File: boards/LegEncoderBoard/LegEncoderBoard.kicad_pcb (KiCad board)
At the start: 2 copper layers, 34 x 42.5 mm, 5 parts, among them J1 S6B-PH-SM4-TB

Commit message: Pre-final leg encoder board
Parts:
- removed ENC1: AS5045-ASST, AS5045:SSOP16_AS5040-ASST_AMS
- added R1: 4.7K, Resistor4.7K:CR0603-FX-4701ELF, F.Cu at (141.8, 104.4)
- added R2: 4.7K, Resistor4.7K:CR0603-FX-4701ELF, F.Cu at (141.8, 103.0)
- added R3: 4.7K, Resistor4.7K:CR0603-FX-4701ELF, F.Cu at (141.8, 105.8)
- added U1: AS5047P-ATST, AS5047P-ASST:AS5047P-ASST, F.Cu at (147.0, 104.9)
- C1: value CC0805KKX5R7BB106 -> 100nF; footprint AS5045-3V3-REG-CAP:CAPC2012X70 -> Capacitor100nF:885342208002
- C2: value CC0805KRX7R7BB104 -> 10nF; footprint AS5045-DECOP-CAP:CC0805N_YAG -> Capacitor10nF:885012206089
- C3: value CC0402KRX7R7BB104 -> 1uF; footprint AS5045-PROG-CAP:YAG_CC0402_YAG -> Capacitor1uF:CC0603JRX7R7BB105
- J1: value S6B-PH-SM4-TB -> Conn_01x05; footprint JST-XH-6:CONN_S6B-XH-SM4-TB_JST -> Connector_JST:JST_XH_B5B-XH-A_1x05_P2.50mm_Vertical
- moved J1 33.5 mm to (142.2, 134.8)
- moved C3 30.4 mm to (153.2, 106.2), turned to 90 degrees
- moved C2 28.1 mm to (151.7, 106.2), turned to -90 degrees
- moved C1 24.0 mm to (153.2, 103.5)
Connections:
- C1 pad 1: GND -> VIN
- C1 pad 2: Net-(ENC1-VDD3V3) -> GND
- C2 pad 1: +5V -> VIN
- C3 pad 1: Net-(ENC1-PROG) -> GND
- C3 pad 2: GND -> VIN
- J1 pad 1: +5V -> VIN
- J1 pad 2: Net-(ENC1-CSN) -> A
- J1 pad 3: Net-(ENC1-CLK) -> B
- J1 pad 4: Net-(ENC1-DO) -> I
- J1 pad 5: Net-(ENC1-PROG) -> GND
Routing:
- net VIN: track 0.00 -> 50.6 mm
- net I: track 0.00 -> 38.2 mm
- net A: track 0.00 -> 36.2 mm
- net Net-(ENC1-PROG): track 33.5 -> 0.00 mm
- net B: track 0.00 -> 31.4 mm
- net +5V: track 28.0 -> 0.00 mm
- net Net-(ENC1-CSN): track 18.7 -> 0.00 mm
- net Net-(ENC1-CLK): track 17.0 -> 0.00 mm
- net Net-(ENC1-DO): track 15.3 -> 0.00 mm
- net Net-(ENC1-VDD3V3): track 10.7 -> 0.00 mm, vias 2 -> 0
- net GND: track 10.1 -> 0.00 mm, vias 3 -> 0
- net MOSI: track 0.00 -> 2.01 mm
- net SCK: track 0.00 -> 1.99 mm
- net CS: track 0.00 -> 1.70 mm
- added copper zone on F.Cu, net GND
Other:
- board size 34 x 42.5 mm -> 76.2 x 76.2 mm
- board text removed: "5V"
- board text removed: "CK"
- board text removed: "CS"
- board text removed: "DI"
- board text removed: "DO"
- board text removed: "GND"

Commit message: Leg encoder board pre-final
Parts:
- added C4: 0.1uF, Capacitor0.1uF:GRM188R71H104KA93J, F.Cu at (137.7, 106.2)
- added C5: 1uF, Capacitor1uF:CC0603JRX7R7BB105, F.Cu at (129.1, 111.1)
- added C6: 1uF, Capacitor1uF:CC0603JRX7R7BB105, F.Cu at (155.8, 111.1)
- added C7: 1uF, Capacitor1uF:CC0603JRX7R7BB105, F.Cu at (142.4, 111.1)
- added CR1: BAT54, EnvelopeDiode:BAT54WS-7-F, F.Cu at (129.4, 114.2)
- added CR2: BAT54, EnvelopeDiode:BAT54WS-7-F, F.Cu at (156.1, 114.3)
- added CR3: BAT54, EnvelopeDiode:BAT54WS-7-F, F.Cu at (142.7, 114.2)
- added D1: REDLED, RedLED:RC0603FR-07150RL, F.Cu at (147.1, 89.5)
- added D2: BLUELED, BlueLED:150080BS75000_Modified, F.Cu at (137.9, 89.5)
- added D3: BLUELED, BlueLED:150080BS75000_Modified, F.Cu at (156.2, 89.5)
- added H1: MountingHole, MountingHole:MountingHole_2.5mm_Pad, F.Cu at (126.1, 83.9)
- added H2: MountingHole, MountingHole:MountingHole_2.5mm_Pad, F.Cu at (168.1, 83.9)
- added H3: MountingHole, MountingHole:MountingHole_2.5mm_Pad, F.Cu at (126.1, 125.9)
- added H4: MountingHole, MountingHole:MountingHole_2.5mm_Pad, F.Cu at (168.1, 125.9)
- added Q1: MMBT3904, Transistor:MMBT3904LT1G, F.Cu at (137.6, 111.1)
- added Q2: MMBT3904, Transistor:MMBT3904LT1G, F.Cu at (164.3, 111.1)
- added Q3: MMBT3904, Transistor:MMBT3904LT1G, F.Cu at (151.0, 111.1)
- added R10: 100K, Resistor100K:CRCW0603100KFKEA, F.Cu at (144.4, 111.1)
- added R11: 47K, Resistor47K:RC0603FR-0747KL, F.Cu at (146.2, 111.1)
- added R12: 470K, Resistor470K:RC0603FR-07470KL, F.Cu at (147.8, 111.1)
- added R13: 22R, Resistor22:RC0603FR-0722RL, F.Cu at (133.9, 106.3)
- added R14: 22R, Resistor22:RC0603FR-0722RL, F.Cu at (133.9, 103.1)
- added R15: 22R, Resistor22:RC0603FR-0722RL, F.Cu at (133.9, 104.7)
- added R4: 1K, Resistor1K:RCG06031K00FKEA, F.Cu at (146.8, 114.2)
- added R5: 100K, Resistor100K:CRCW0603100KFKEA, F.Cu at (157.8, 111.1)
- added R6: 150R, Resistor150:RESC1607X60N, F.Cu at (133.6, 114.2)
- added R7: 47K, Resistor47K:RC0603FR-0747KL, F.Cu at (159.5, 111.1)
- added R8: 470K, Resistor470K:RC0603FR-07470KL, F.Cu at (161.1, 111.1)
- added R9: 150R, Resistor150:RESC1607X60N, F.Cu at (160.2, 114.3)
- added U2: SN74LVC3G17DCUR, SchmittBuffer:SN74LVC3G17DCUR, F.Cu at (137.7, 103.8)
- J1: footprint Connector_JST:JST_XH_B5B-XH-A_1x05_P2.50mm_Vertical -> Connector_IDC:IDC-Header_2x04_P2.54mm_Vertical
- R1: value 4.7K -> 100K; footprint Resistor4.7K:CR0603-FX-4701ELF -> Resistor100K:CRCW0603100KFKEA
- R2: value 4.7K -> 47K; footprint Resistor4.7K:CR0603-FX-4701ELF -> Resistor47K:RC0603FR-0747KL
- R3: value 4.7K -> 470K; footprint Resistor4.7K:CR0603-FX-4701ELF -> Resistor470K:RC0603FR-07470KL
- moved J1 13.2 mm to (151.1, 125.1), turned to -90 degrees
- moved R1 12.6 mm to (131.0, 111.1), turned to -90 degrees
- moved R2 12.0 mm to (132.8, 111.1), turned to -90 degrees
- moved R3 9.13 mm to (134.4, 111.1), turned to -90 degrees
- moved C3 1.01 mm to (154.2, 106.3)
- moved C2 0.81 mm to (152.4, 106.4)
- moved C1 0.80 mm to (154.0, 103.5)
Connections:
- J1 pad 2: A -> GND
- J1 pad 3: B -> /A_OUT
- J1 pad 4: I -> GND
- J1 pad 5: GND -> /B_OUT
- R1 pad 1: SCK -> /A_ENV
- R2 pad 1: VIN -> /A_ENV
- R2 pad 2: CS -> /A_BASE
- R3 pad 1: MOSI -> /A_BASE
- U1 pad 1: CS -> VIN
- U1 pad 2: SCK -> GND
- U1 pad 3: MISO -> unconnected-(U1-MISO-Pad3)
- U1 pad 4: MOSI -> GND
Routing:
- net VIN: track 50.6 -> 95.2 mm, vias 0 -> 1
- net /A_OUT: track 0.00 -> 37.2 mm
- net /B_OUT: track 0.00 -> 37.0 mm, vias 0 -> 1
- net A_BUF: track 0.00 -> 33.9 mm, vias 0 -> 2
- net B_BUF: track 0.00 -> 31.0 mm, vias 0 -> 2
- net /A_LED_ANODE: track 0.00 -> 29.0 mm, vias 0 -> 2
- net /I_OUT: track 0.00 -> 28.8 mm, vias 0 -> 1
- net A: track 36.2 -> 9.26 mm
- net /B_LED_ANODE: track 0.00 -> 26.7 mm, vias 0 -> 2
- net /B_LED_CATHODE: track 0.00 -> 25.8 mm
- net /A_LED_CATHODE: track 0.00 -> 25.5 mm, vias 0 -> 2
- net /I_LED_ANODE: track 0.00 -> 25.2 mm, vias 0 -> 2
- net GND: track 0.00 -> 25.2 mm, vias 0 -> 13
- net B: track 31.4 -> 6.73 mm
- net /I_LED_CATHODE: track 0.00 -> 23.9 mm
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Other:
- board size 76.2 x 76.2 mm -> 66 x 66 mm
- board text added: "3V3"
- board text added: "A"
- board text added: "B"
- board text added: "GND"
- board text added: "I"

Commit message: Prepare encoder boards for manufacturing
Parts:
- C1: footprint Capacitor100nF:885342208002 -> Capacitor100nF:CC0603KRX7R9BB104
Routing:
- net VIN: track 95.2 -> 96.2 mm
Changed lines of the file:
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@@
 			)
 		)
-		(property "LCSC" "C2169542"
+		(property "LCSC" "C85973"
 			(at 0 0 0)
 			(layer "F.SilkS")
@@
 		(embedded_fonts no)
 	)
-	(footprint "Capacitor100nF:885342208002"
+	(footprint "Capacitor100nF:CC0603KRX7R9BB104"
 		(layer "F.Cu")
 		(at 154 103.55)
+		(tags "CC0603KRX7R9BB104 ")
 		(property "Reference" "C1"
-			(at 0 -1.6032 0)
+			(at 0 0 0)
+			(unlocked yes)
 			(layer "F.SilkS")
 			(hide yes)
 			(effects
 				(font
-					(size 0.32 0.32)
-					(thickness 0.08)
+					(size 1 1)
+					(thickness 0.15)
 				)
 			)
 		)
 		(property "Value" "100nF"
-			(at -0.1 1.3968 0)
+			(at 0 0 0)
+			(unlocked yes)
 			(layer "F.Fab")
 			(hide yes)
 			(effects
 				(font
-					(size 0.32 0.32)
-					(thickness 0.08)
+					(size 1 1)
+					(thickness 0.15)
 				)
 			)
@@
 		(property "LCSC" "C2176910"
 			(at 0 0 0)
-			(layer "F.SilkS")
+			(unlocked yes)
+			(layer "F.Fab")
 			(hide yes)
 			(effects
 				(font
-					(size 1.27 1.27)
+					(size 1 1)
 					(thickness 0.15)
 				)
@@
 		(attr smd)
 		(fp_line
-			(start -0.8 -0.9)
-			(end 0.8 -0.9)
+			(start -1.1049 -0.5334)
+			(end 1.1049 -0.5334)
 			(stroke
-				(width 0.2)
+				(width 0.1524)
 				(type solid)
 			)
-			(layer "F.SilkS")
+			(layer "F.CrtYd")
 		)
 		(fp_line
-			(start 0.8 0.9)
-			(end -0.8 0.9)
+			(start -1.1049 0.5334)
+			(end -1.1049 -0.5334)
 			(stroke
-				(width 0.2)
+				(width 0.1524)
 				(type solid)
 			)
-			(layer "F.SilkS")
+			(layer "F.CrtYd")
 		)
-		(fp_poly
-			(pts
-				(xy -2.2 -1.1) (xy 2.2 -1.1) (xy 2.2 1.1) (xy -2.2 1.1)
+		(fp_line
+			(start 1.1049 -0.5334)
+			(end 1.1049 0.5334)
+			(stroke
+				(width 0.1524)
+				(type solid)
 			)
+			(layer "F.CrtYd")
+		)
+		(fp_line
+			(start 1.1049 0.5334)
+			(end -1.1049 0.5334)
 			(stroke
-				(width 0.1)
+				(width 0.1524)
 				(type solid)
 			)
-			(fill yes)
 			(layer "F.CrtYd")
 		)
 		(fp_line
-			(start -1.6 -0.8)
-			(end -1.6 0.8)
+			(start -0.8509 -0.4572)
+			(end -0.8509 0.4572)
 			(stroke
-				(width 0.1)
+				(width 0.0254)
 				(type solid)
 			)
@@
 		)
 		(fp_line
-			(start -1.6 -0.8)
-			(end 1.6 -0.8)
+			(start -0.8509 -0.4572)
+			(end -0.8509 0.4572)
 			(stroke
-				(width 0.1)
+				(width 0.0254)
 				(type solid)
 			)
@@
 		)
 		(fp_line
-			(start -1.6 0.8)
-			(end 1.6 0.8)
+			(start -0.8509 0.4572)
+			(end -0.2413 0.4572)
 			(stroke
-				(width 0.1)
+				(width 0.0254)
 				(type solid)
 			)
@@
 		)
 		(fp_line
-			(start 1.6 0.8)
-			(end 1.6 -0.8)
+			(start -0.8509 0.4572)
+			(end 0.8509 0.4572)
 			(stroke
-				(width 0.1)
+				(width 0.0254)
+				(type solid)
+			)
+			(layer "F.Fab")
+		)
+		(fp_line
+			(start -0.2413 -0.4572)
+			(end -0.8509 -0.4572)
+			(stroke
+				(width 0.0254)
+				(type solid)
+			)
+			(layer "F.Fab")
+		)
+		(fp_line
+			(start -0.2413 0.4572)
+			(end -0.2413 -0.4572)
+			(stroke
+				(width 0.0254)
+				(type solid)
+			)
+			(layer "F.Fab")
+		)
+		(fp_line
+			(start 0.2413 -0.4572)
+			(end 0.2413 0.4572)
+			(stroke
+				(width 0.0254)
+				(type solid)
+			)
+			(layer "F.Fab")
+		)
+		(fp_line
+			(start 0.2413 0.4572)
+			(end 0.8509 0.4572)
+			(stroke
+				(width 0.0254)
 				(type solid)
 			)
 			(layer "F.Fab")
 		)
+		(fp_line
+			(start 0.8509 -0.4572)
+			(end -0.8509 -0.4572)
+			(stroke
+				(width 0.0254)
+				(type solid)
+			)
+			(layer "F.Fab")
+		)
+		(fp_line
+			(start 0.8509 -0.4572)
+			(end 0.2413 -0.4572)
+			(stroke
+				(width 0.0254)
+				(type solid)
+			)
+			(layer "F.Fab")
+		)
+		(fp_line
+			(start 0.8509 0.4572)
+			(end 0.8509 -0.4572)
+			(stroke
+				(width 0.0254)
+				(type solid)
+			)
+			(layer "F.Fab")
+		)
+		(fp_line
+			(start 0.8509 0.4572)
+			(end 0.8509 -0.4572)
+			(stroke
+				(width 0.0254)
+				(type solid)
+			)
+			(layer "F.Fab")
+		)
+		(fp_text user "${REFERENCE}"
+			(at 0 0 0)
+			(unlocked yes)
+			(layer "F.Fab")
+			(effects
+				(font
+					(size 1 1)
+					(thickness 0.15)
+				)
+			)
+		)
 		(pad "1" smd rect
-			(at -1.55 0)
-			(size 0.9 1.6)
+			(at -0.6223 0)
+			(size 0.762 0.8636)
 			(layers "F.Cu" "F.Mask" "F.Paste")
 			(net 2 "VIN")
 			(pintype "passive")
-			(solder_mask_margin 0.102)
 		)
 		(pad "2" smd rect
-			(at 1.55 0)
-			(size 0.9 1.6)
+			(at 0.6223 0)
+			(size 0.762 0.8636)
 			(layers "F.Cu" "F.Mask" "F.Paste")
 			(net 7 "GND")
 			(pintype "passive")
-			(solder_mask_margin 0.102)
+		)
+		(zone
+			(net 0)
+			(net_name "")
+			(layer "F.Cu")
+			(hatch full 0.508)
+			(connect_pads
+				(clearance 0)
+			)
+			(min_thickness 0.254)
+			(filled_areas_thickness no)
+			(keepout
+				(tracks not_allowed)
+				(vias not_allowed)
+				(pads allowed)
+				(copperpour not_allowed)
+				(footprints allowed)
+			)
+			(placement
+				(enabled no)
+				(sheetname "")
+			)
+			(fill
+				(thermal_gap 0.508)
+				(thermal_bridge_width 0.508)
+			)
+			(polygon
+				(pts
+					(xy 153.8095 103.1436) (xy 154.1905 103.1436) (xy 154.1905 103.9564) (xy 153.8095 103.9564)
+				)
+			)
 		)
 		(embedded_fonts no)
-		(model "${KIPRJMOD}/dependencies/Capacitor100nF/885342208002.step"
+		(model "${KIPRJMOD}/dependencies/Capacitor100nF/CC0603KRX7R9BB104.step"
 			(offset
 				(xyz 0 0 0)
@@
 		(sheetname "/")
 		(sheetfile "LegEncoderBoard.kicad_sch")
-		(attr through_hole)
+		(attr through_hole exclude_from_pos_files exclude_from_bom)
 		(fp_line
 			(start -3.29 12.83)
@@
 		(width 0.25)
 		(layer "F.Cu")
+		(net 2)
+	)
+	(segment
+		(start 152.45 103.55)
+		(end 153.3777 103.55)
+		(width 0.25)
+		(layer "F.Cu")

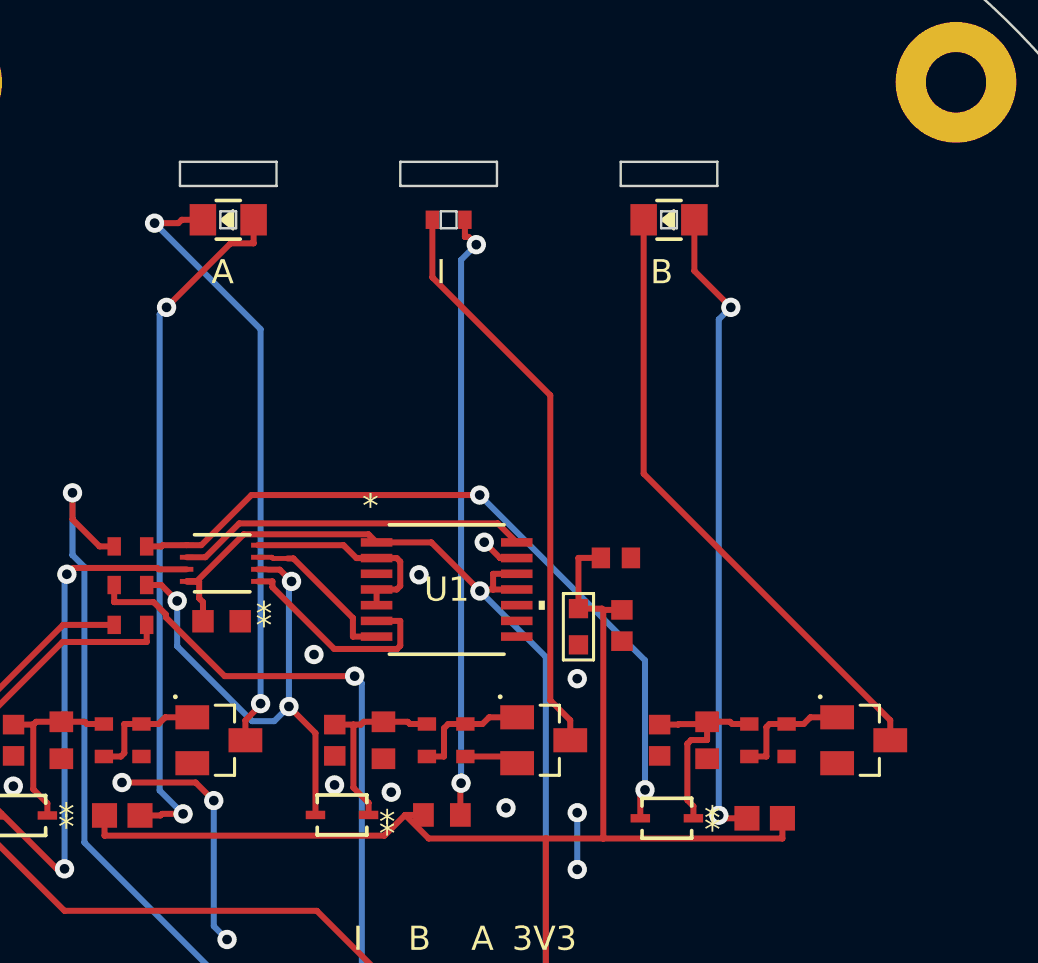
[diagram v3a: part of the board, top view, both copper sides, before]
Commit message: Pre-flight on two encoder boards
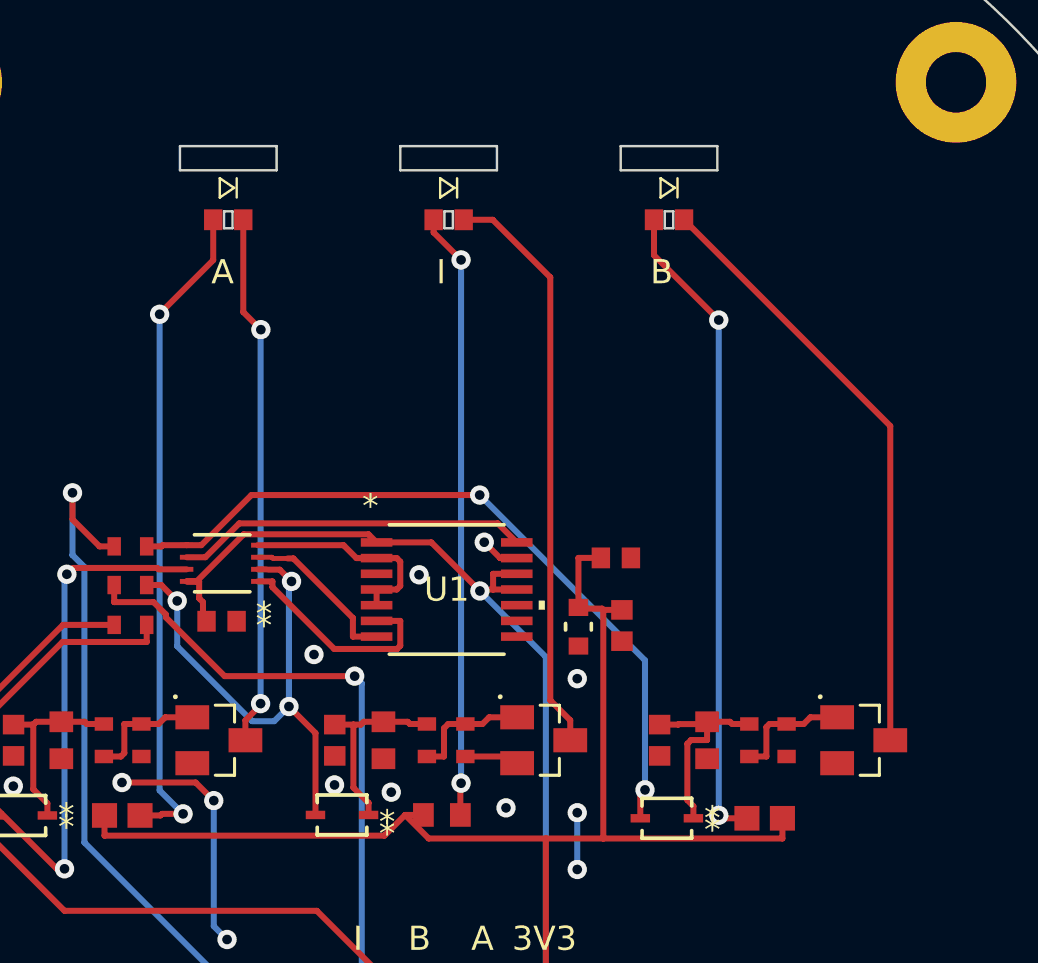
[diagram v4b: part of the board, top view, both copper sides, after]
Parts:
- C2: footprint Capacitor10nF:885012206089 -> Capacitor10nF:GRM1885C1H103JA01D
- C4: value 0.1uF -> 100nF; footprint Capacitor0.1uF:GRM188R71H104KA93J -> Capacitor100nF:CC0603KRX7R9BB104
- D1: footprint RedLED:RC0603FR-07150RL -> LedRed:YLED0603R
- D2, D3: footprint BlueLED:150080BS75000_Modified -> LedBlue:YLED0603B
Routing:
- net /A_LED_CATHODE: track 25.5 -> 22.1 mm
- net /A_LED_ANODE: track 29.0 -> 27.9 mm
- net /B_LED_CATHODE: track 25.8 -> 25.1 mm
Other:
- outline, holes or cut-outs redrawn

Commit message: Ordered leg encoder board
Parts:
- D1: footprint LedRed:YLED0603R -> LedRed:NCD0603R1
- D2, D3: footprint LedBlue:YLED0603B -> LedBlue:150080BS75000_Modified
- U2: value SN74LVC3G17DCUR -> SN74LVC3G17DCTR; footprint SchmittBuffer:SN74LVC3G17DCUR -> SchmittBuffer:SN74LVC3G17DCTR
- moved R15 6.49 mm to (140.1, 106.8)
- moved C4 3.85 mm to (133.8, 105.7), turned to 0 degrees
- moved R13 2.20 mm to (133.8, 104.1)
- moved U2 0.75 mm to (138.4, 103.8)
- moved R14 0.50 mm to (133.8, 102.6)
- turned D1 to 180 degrees
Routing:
- net GND: track 25.2 -> 46.3 mm, vias 13 -> 14
- net A_BUF: track 33.9 -> 17.4 mm, vias 2 -> 0
- net VIN: track 96.2 -> 83.2 mm, vias 1 -> 0
- net I_BUF: track 21.3 -> 12.3 mm, vias 3 -> 0
- net /I_OUT: track 28.8 -> 20.1 mm
- net /A_LED_CATHODE: track 22.1 -> 28.5 mm
- net /A_OUT: track 37.2 -> 32.8 mm, vias 0 -> 1
- net /A_LED_ANODE: track 27.9 -> 31.8 mm
- net B_BUF: track 31.0 -> 33.8 mm, vias 2 -> 0
- net /I_BASE: track 5.09 -> 7.03 mm
- net /B_LED_ANODE: track 27.0 -> 28.7 mm
- net /I_ENV: track 7.90 -> 9.27 mm
- net A: track 9.26 -> 7.99 mm
- net /I_LED_ANODE: track 25.1 -> 26.1 mm
- net B: track 6.73 -> 6.00 mm
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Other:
- outline, holes or cut-outs redrawn

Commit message: Finalize leg encoder board iteration
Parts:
- added C10: 10nF, Capacitor10nF:GRM1885C1H103JA01D, F.Cu at (140.7, 117.5)
- added C8: 10nF, Capacitor10nF:GRM1885C1H103JA01D, F.Cu at (132.9, 117.5)
- added C9: 10nF, Capacitor10nF:GRM1885C1H103JA01D, F.Cu at (165.4, 117.5)
- added CR4: BAT54, EnvelopeDiode:BAT54WS-7-F, F.Cu at (129.2, 117.5)
- added CR5: BAT54, EnvelopeDiode:BAT54WS-7-F, F.Cu at (161.6, 117.5)
- added CR6: BAT54, EnvelopeDiode:BAT54WS-7-F, F.Cu at (136.9, 117.5)
- added J2: Conn_01x04, Connector_JST:JST_XH_B4B-XH-A_1x04_P2.50mm_Vertical, F.Cu at (143.3, 81.6)
- added R16: 100K, Resistor100K:CRCW0603100KFKEA, F.Cu at (131.1, 117.5)
- added R17: 100K, Resistor100K:CRCW0603100KFKEA, F.Cu at (163.6, 117.5)
- added R18: 100K, Resistor100K:CRCW0603100KFKEA, F.Cu at (138.9, 117.5)
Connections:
- CR1 pad 2: A_BUF -> /A_PULSE
- CR2 pad 2: B_BUF -> /B_PULSE
- CR3 pad 2: I_BUF -> /I_PULSE
- U1 pad 1: VIN -> CS
- U1 pad 2: GND -> CLK
- U1 pad 3: unconnected-(U1-MISO-Pad3) -> MISO
- U1 pad 4: GND -> MOSI
- U1 pad 6: A -> B
- U1 pad 7: B -> A
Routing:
- net CLK: track 0.00 -> 56.8 mm, vias 0 -> 1
- net MOSI: track 0.00 -> 31.5 mm, vias 0 -> 1
- net MISO: track 0.00 -> 30.3 mm, vias 0 -> 1
- net CS: track 0.00 -> 25.1 mm, vias 0 -> 2
- net B_BUF: track 33.8 -> 54.2 mm, vias 0 -> 2
- net /B_PULSE: track 0.00 -> 14.0 mm, vias 0 -> 2
- net GND: track 46.3 -> 58.5 mm, vias 14 -> 19
- net /I_PULSE: track 0.00 -> 10.5 mm
- net I_BUF: track 12.3 -> 21.3 mm, vias 0 -> 2
- net /A_PULSE: track 0.00 -> 8.66 mm, vias 0 -> 2
- net A_BUF: track 17.4 -> 25.6 mm
- net A: track 7.99 -> 4.73 mm
- net /A_OUT: track 32.8 -> 34.9 mm
- net VIN: track 83.2 -> 84.5 mm
- net /A_LED_ANODE: track 31.8 -> 33.0 mm
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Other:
- board text added: "CLK"
- board text added: "CS"
- board text added: "MISO"
- board text added: "MOSI"

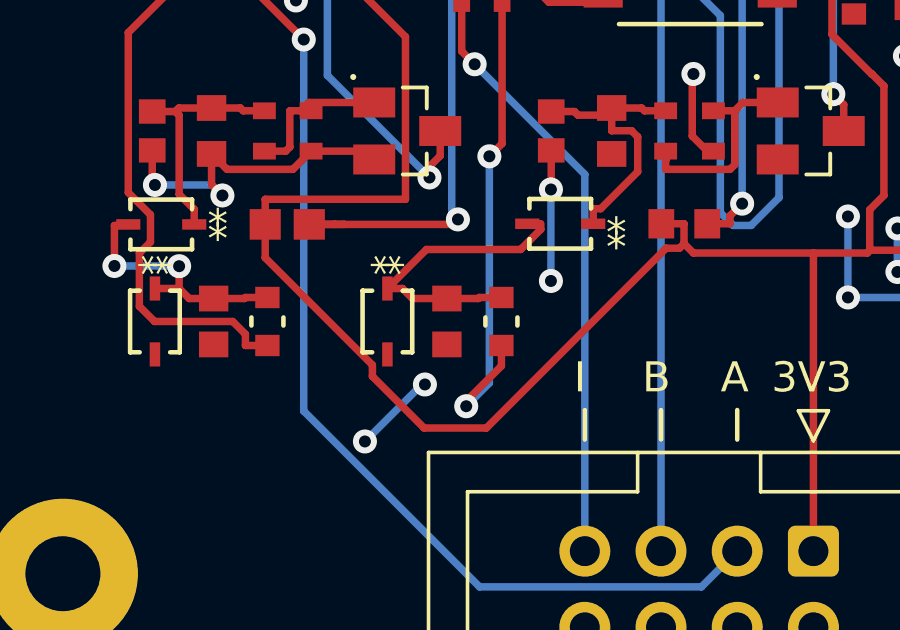
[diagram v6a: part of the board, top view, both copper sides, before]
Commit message: Debug and re-design leg encoder and leg robot board
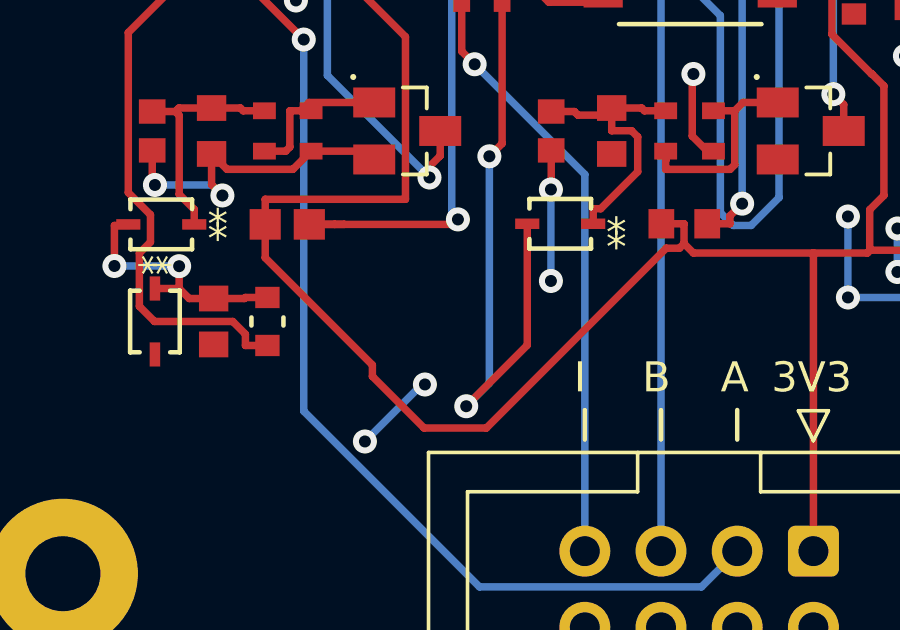
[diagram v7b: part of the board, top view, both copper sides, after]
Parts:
- removed C10: 10nF, Capacitor10nF:GRM1885C1H103JA01D
- removed CR6: BAT54, EnvelopeDiode:BAT54WS-7-F
- removed R18: 100K, Resistor100K:CRCW0603100KFKEA
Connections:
- CR3 pad 2: /I_PULSE -> I_BUF
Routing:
- net /I_PULSE: track 10.5 -> 0.00 mm
- net I_BUF: track 21.3 -> 25.9 mm
